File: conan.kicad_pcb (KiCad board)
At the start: 4 copper layers, 313 parts, among them J1 JST-XH, J10 PWM11, J11 PWM3, J12 PWM7, J13 PWM12, J14 PWM4, J15 PWM8, J16 Stepper, J17 Stepper, J18 Stepper, J19 Stepper, J2 JST-XH, J20 Stepper, J21 Stepper, J22 Boot, J23 UART1, J24 UART2, J25 USB_B_Micro, J26 Endstop 1, J27 Endstop 2, J28 Endstop 3, J29 Endstop 4, J3 JTAG, J30 Endstop 5, J31 Endstop 6, J32 Endstop 7, J33 Endstop 8, J34 Watchdog, J35 Thermistor 1, J36 Thermistor 2, J37 Thermistor 3, J38 Thermistor 4, J39 Thermistor 5, J4 PWM9, J40 Thermistor 6, J43 pmod, J44 esp8266, J45 Chain_in, J46 Chain_out, J47 Exp1_L, J48 Display, J49 Exp1_R, J5 PWM5, J50 Vaux in, J51 VM2 in, J52 VM1 in, J53 Vaux in, J54 Exp2_L, J55 Exp2_R, J6 PWM1_HP, J7 PWM10, J8 PWM2_HP, J9 PWM6, Q1 AON7524, Q2 TPH1R405PL, Q3 TPH1R405PL, Q4 AON7524, Q5 AON7524, Q6 AON7524, Q7 AON7524, Q8 AON7524, Q9 Q_NMOS_DGS, SW1 Reset, U1 ECP5U12_CABGA256, U10 TMC2209, U11 TMC2209, U12 TMC2209, U13 TMC2209, U14 AT25xxx, U15 STM32F070CBTx, U16 74VLX244, U17 STWD100, U2 L7986, U3 TLV62569, U4 TLV62569, U5 LP5907MFX-2.5, U6 LP5907MFX-3.3, U7 MIC4127, U8 TMC2209, U9 TMC2209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

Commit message: 2./3. driver in progress
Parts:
- moved C52 8.48 mm to (98.4, 32.8), turned to 0 degrees
- moved C62 7.73 mm to (86.0, 37.4), turned to 270 degrees
- moved C56 3.47 mm to (100.4, 37.4)
- moved C54 3.25 mm to (98.8, 40.0), turned to 270 degrees
- moved C58 3.16 mm to (76.6, 32.8), turned to 180 degrees
- moved C60 2.63 mm to (84.4, 40.0), turned to 270 degrees
- moved C59 2.39 mm to (84.0, 32.8), turned to 0 degrees
- moved C53 2.38 mm to (91.0, 32.8), turned to 180 degrees
- moved R35 1.52 mm to (83.6, 30.8)
- moved R34 1.47 mm to (77.0, 30.8)
- moved R31 1.31 mm to (91.4, 30.8)
- moved C55 1.07 mm to (95.8, 41.0)
- moved C51 0.86 mm to (94.8, 45.1)
- moved U8 0.72 mm to (94.7, 36.7)
- moved C61 0.63 mm to (81.4, 41.0)
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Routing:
- net GND: track 76.9 -> 134.9 mm, vias 38 -> 41
- net ENN: track 16.4 -> 43.0 mm
- net /Stepper/Stepper 3/OA2: track 0.00 -> 20.2 mm
- net /Stepper/Stepper 3/VM: track 4.19 -> 22.5 mm, vias 0 -> 3
- net /Stepper/Stepper 2/OA2: track 5.88 -> 20.2 mm, vias 1 -> 0
- net CLK: track 9.30 -> 21.6 mm
- net /Stepper/Stepper 3/OB2: track 0.00 -> 11.5 mm
- net DIR3: track 2.20 -> 11.5 mm
- net DIR2: track 3.77 -> 13.0 mm
- net /Stepper/Stepper 3/OA1: track 0.00 -> 9.08 mm
- net STEP2: track 3.97 -> 12.5 mm
- net STEP3: track 3.77 -> 12.3 mm
- net /Stepper/Stepper 3/OB1: track 0.00 -> 7.28 mm
- net /Stepper/Stepper 1/VM: track 18.3 -> 25.4 mm, vias 3 -> 9
- net INDEX3: track 3.17 -> 9.58 mm
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- removed copper zone on In2.Cu, net /Stepper/Stepper 2/VM
- removed copper zone on F.Cu, net GND

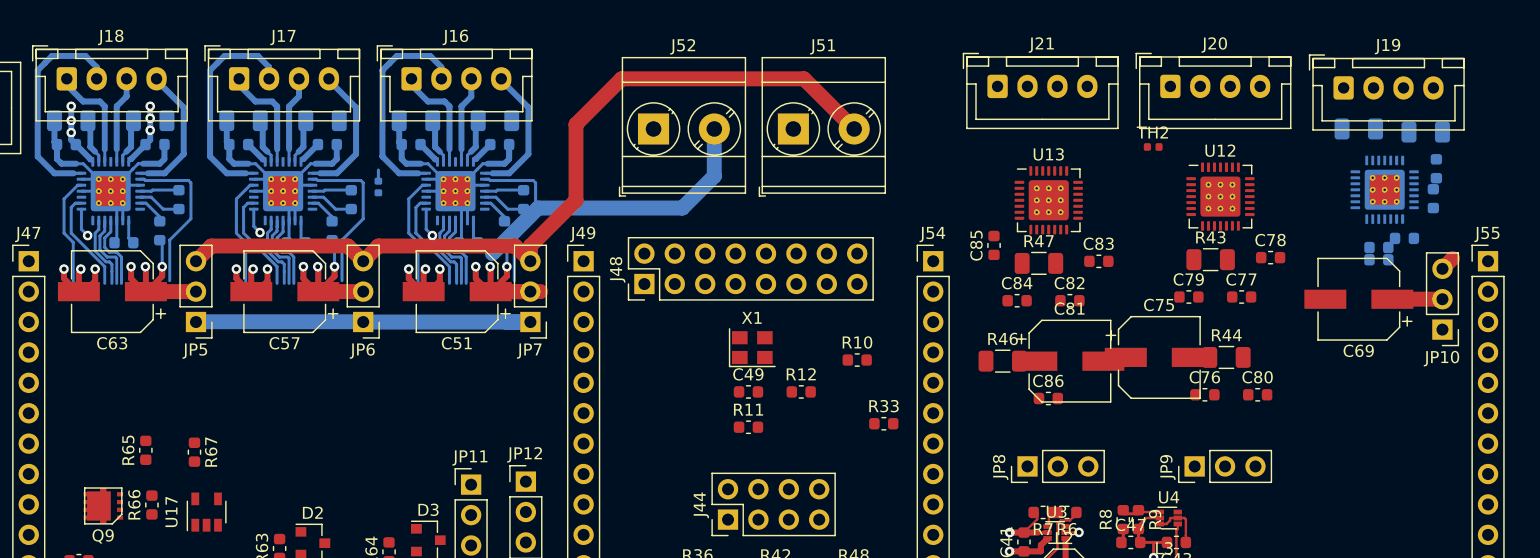
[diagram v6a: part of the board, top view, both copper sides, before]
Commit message: stepper driver done
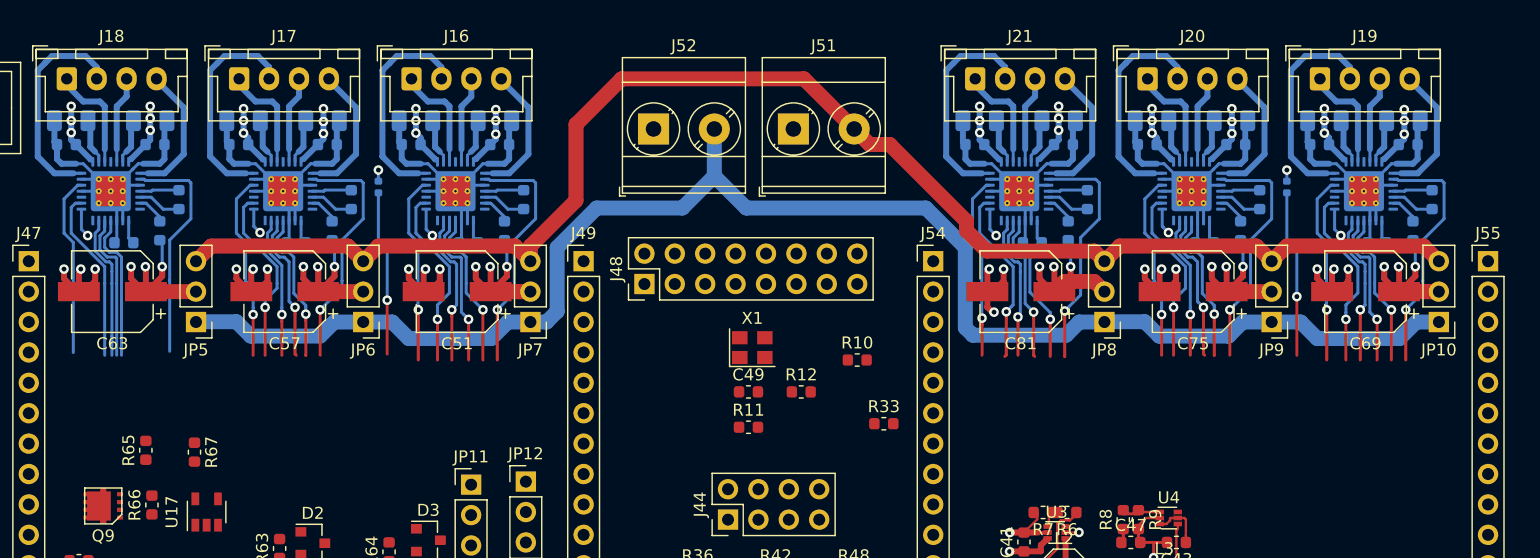
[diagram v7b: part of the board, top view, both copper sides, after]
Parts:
- C76, C77, C78, C79, C80, C82, C83, C84, C85, C86, R43, R44, R46, R47, TH2, U12, U13: moved to B.Cu
- moved C76 21.1 mm to (159.9, 32.8)
- moved R46 20.2 mm to (138.5, 30.8), turned to 180 degrees
- moved R44 19.8 mm to (159.5, 30.8)
- moved C86 16.9 mm to (147.5, 37.4), turned to 270 degrees
- moved C80 16.3 mm to (161.9, 37.4), turned to 270 degrees
- moved C77 15.0 mm to (152.5, 32.8), turned to 180 degrees
- moved C83 14.2 mm to (138.1, 32.8), turned to 180 degrees
- moved JP8 13.7 mm to (148.9, 47.6), turned to 180 degrees
- moved JP9 13.7 mm to (162.9, 47.6), turned to 180 degrees
- moved C82 13.1 mm to (145.5, 32.8)
- moved R43 12.6 mm to (152.9, 30.8), turned to 180 degrees
- moved R47 12.0 mm to (145.1, 30.8)
- moved TH2 11.7 mm to (164.2, 36.3), turned to 270 degrees
- moved C71 10.8 mm to (166.9, 32.8)
- moved C70 8.94 mm to (174.3, 32.8), turned to 0 degrees
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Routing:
- net GND: track 134.9 -> 251.4 mm, vias 41 -> 52
- net ENN: track 43.0 -> 123.9 mm, vias 0 -> 5
- net +VM1: track 55.2 -> 130.1 mm
- net CLK: track 21.6 -> 76.8 mm, vias 0 -> 5
- net +VM2: track 70.8 -> 125.6 mm
- net /Stepper/Stepper 4/VM: track 0.00 -> 26.1 mm, vias 0 -> 9
- net /Stepper/Stepper 5/VM: track 0.00 -> 24.3 mm, vias 0 -> 9
- net /Stepper/Stepper 6/VM: track 4.19 -> 27.9 mm, vias 0 -> 9
- net /Stepper/Stepper 6/OA2: track 0.00 -> 20.2 mm
- net /Stepper/Stepper 5/OA2: track 0.00 -> 20.2 mm
- net /Stepper/Stepper 4/OA2: track 0.00 -> 20.2 mm
- net DIR6: track 3.17 -> 18.9 mm, vias 0 -> 1
- net DIR5: track 2.20 -> 17.9 mm, vias 0 -> 1
- net STEP6: track 3.77 -> 19.1 mm, vias 1 -> 2
- net DIR4: track 3.17 -> 18.5 mm, vias 0 -> 1
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- added copper zone on In2.Cu, net /Stepper/Stepper 2/VM
- added copper zone on In2.Cu, net /Stepper/Stepper 3/VM
- added copper zone on In2.Cu, net /Stepper/Stepper 4/VM
- added copper zone on In2.Cu, net /Stepper/Stepper 5/VM
- added copper zone on In2.Cu, net /Stepper/Stepper 6/VM

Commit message: dc-dc converter
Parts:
- C50: moved to B.Cu
- Q2, Q3: footprint Package_SO:SSOP-8_5.25x5.24mm_P1.27mm -> arne:TPH1R405PL
- moved J34 54.3 mm to (29.0, 78.7)
- moved D1 32.8 mm to (159.2, 62.1), turned to 90 degrees
- moved C42 28.4 mm to (152.6, 56.9), turned to 90 degrees
- moved L1 28.3 mm to (170.4, 63.6), turned to 90 degrees
- moved C40 26.9 mm to (166.6, 54.5), turned to 180 degrees
- moved C46 26.2 mm to (146.6, 57.0), turned to 90 degrees
- moved U5 22.9 mm to (149.6, 56.9), turned to 180 degrees
- moved R5 21.7 mm to (157.6, 69.2), turned to 270 degrees
- moved R2 18.1 mm to (162.8, 75.3)
- moved U2 17.8 mm to (167.4, 74.6), turned to 270 degrees
- moved R4 17.3 mm to (161.9, 68.3), turned to 180 degrees
- moved C37 17.3 mm to (163.6, 72.7), turned to 270 degrees
- moved J1 16.7 mm to (192.6, 86.4)
- moved J2 16.7 mm to (192.6, 95.6)
- moved C29 16.6 mm to (169.6, 81.9), turned to 180 degrees
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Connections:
- U7 pad 9: (no net) -> GND
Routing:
- net CLK: track 76.8 -> 135.9 mm, vias 5 -> 9
- net ENN: track 123.9 -> 177.8 mm, vias 5 -> 10
- net +5V: track 9.56 -> 47.6 mm, vias 2 -> 14
- net GND: track 251.4 -> 283.2 mm, vias 52 -> 117
- net +2V5: track 1.13 -> 26.0 mm, vias 2 -> 6
- net Net-(R97-Pad2): track 0.00 -> 20.3 mm, vias 0 -> 3
- net Net-(Q3-Pad2): track 0.00 -> 18.7 mm, vias 0 -> 2
- net Net-(D1-Pad1): track 0.00 -> 18.3 mm
- net +Vaux: track 0.00 -> 16.7 mm, vias 0 -> 6
- net Net-(R39-Pad2): track 0.00 -> 15.3 mm, vias 0 -> 3
- net Net-(R36-Pad2): track 0.00 -> 15.0 mm, vias 0 -> 3
- net Net-(R48-Pad2): track 0.00 -> 14.6 mm, vias 0 -> 3
- net Net-(R45-Pad2): track 0.00 -> 14.6 mm, vias 0 -> 3
- net Net-(R42-Pad2): track 0.00 -> 11.9 mm, vias 0 -> 1
- net Net-(JP1-Pad2): track 0.00 -> 10.4 mm, vias 0 -> 2
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- added copper zone on In2.Cu, net +1V1
- added copper zone on In2.Cu, net +2V5
- added copper zone on In2.Cu, net +3V3
- added copper zone on In2.Cu, net +5V
- added copper zone on B.Cu, net +Vaux
- added copper zone on In2.Cu, net +Vaux
- added copper zone on F.Cu, net GND
- added copper zone on F.Cu, net Net-(J6-Pad1)
- added copper zone on F.Cu, net Net-(J8-Pad1)
